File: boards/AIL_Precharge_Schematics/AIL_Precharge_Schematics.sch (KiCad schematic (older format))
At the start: 16 parts, among them K1 G6C-1117P-US

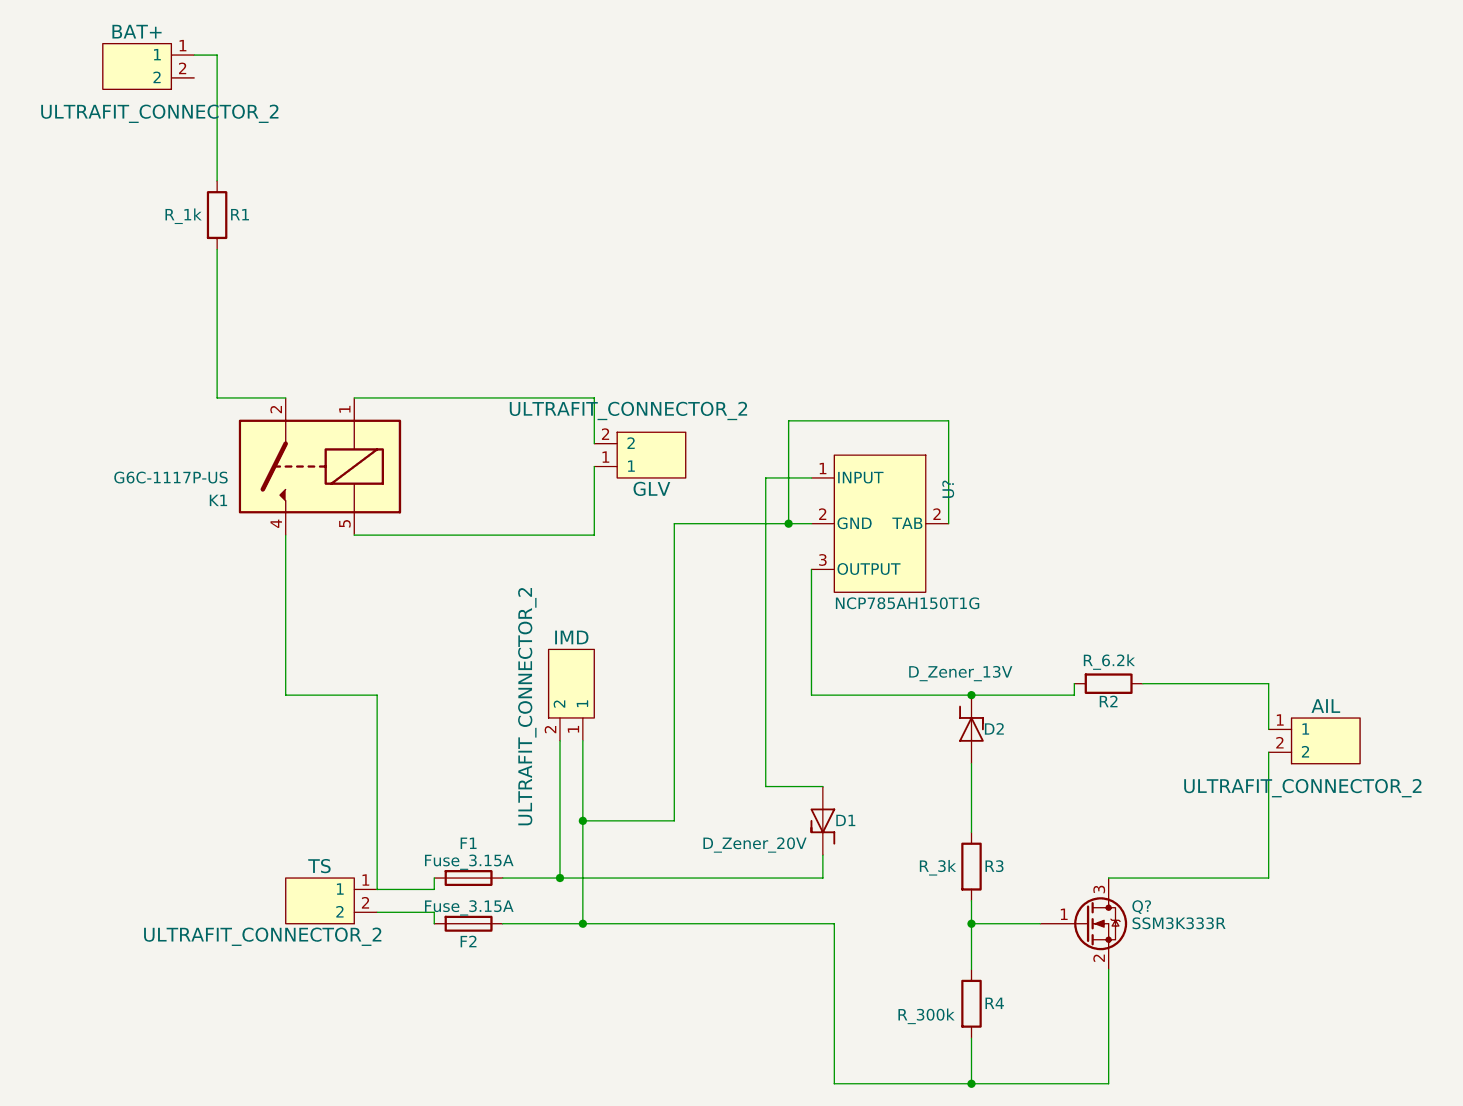
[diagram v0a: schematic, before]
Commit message: add pcb layout with tracing for AIL Precharge
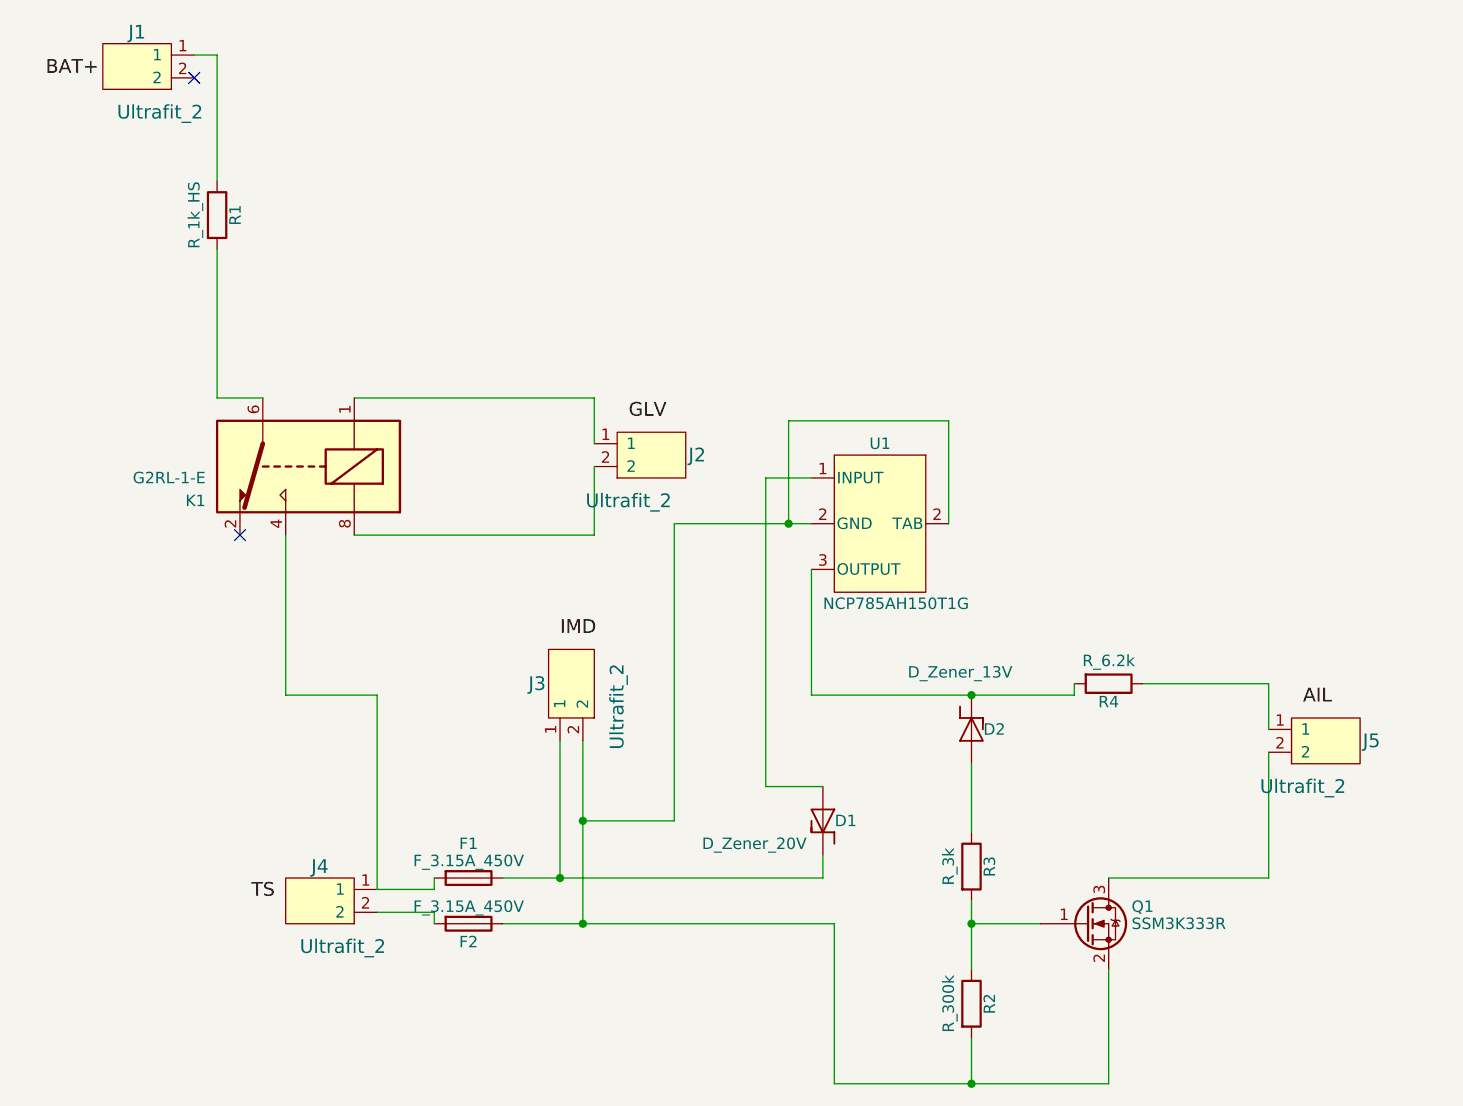
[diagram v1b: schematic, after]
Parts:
- removed AIL, BAT+, GLV, IMD, TS: ULTRAFIT_CONNECTOR_2, symbol ULTRAFIT_CONNECTOR_2
- removed F1, F2: Fuse_3.15A, symbol Fuse
- removed K1: G6C-1117P-US, Relays_THT:Relay_SPDT_OMRON-G5Q, symbol G6C-1117P-US
- removed Q?: SSM3K333R, TO_SOT_Packages_SMD:SOT-23, symbol SSM3K333R
- removed R1: R_1k, Resistors_SMD:R_0805, symbol R_1k
- removed R2: R_6.2k, Resistors_SMD:R_0805, symbol R_6.2k
- removed R4: R_300k, Resistors_SMD:R_0805, symbol R_300k
- removed U?: NCP785AH150T1G, TO_SOT_Packages_SMD:SOT-89-3, symbol NCP785AH150T1G
- added F1, F2: F_3.15A_450V, footprints:Fuse_TE7_Littelfuse-807Series, symbol F_3.15A_450V
- added J1, J2, J3, J4, J5: Ultrafit_2, footprints:Ultrafit_2, symbol Ultrafit_2
- added K1: G2RL-1-E, footprints:Relay_SPDT_OMRON-G2RL-1-E, symbol G2RL-1-E
- added Q1: SSM3K333R, footprints:SOT-23F, symbol SSM3K333R
- added R1: R_1k_HS, footprints:R_1k_HS_TO247, symbol R_1k_HS
- added R2: R_300k, footprints:R_0805_OEM, symbol R_300k
- added R4: R_6.2k, footprints:R_0805_OEM, symbol R_6.2k
- added U1: NCP785AH150T1G, footprints:SOT-89-3, symbol NCP785AH150T1G
- R3: footprint Resistors_SMD:R_0805 -> footprints:R_0805_OEM
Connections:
- net at R3.2: now also Q1.1 (G), R2.1
- net at D2.1 (K): now also R4.2, U1.3 (OUTPUT)
- net at D1.1 (K): now also F1.1, J3.1
- net at D1.2 (A): now also U1.1 (INPUT)
- new net: F1.2, J4.1, K1.4
- new net: F2.1, J3.2, Q1.2 (S), R2.2, U1.2 (TAB)
- new net: F2.2, J4.2
- new net: J1.1, R1.1
- new net: J2.1, K1.1
- new net: J2.2, K1.8
- new net: J5.1, R4.1
- new net: K1.6, R1.2
- new net: J5.2, Q1.3 (D)
- no-connect marks 0 -> 2
